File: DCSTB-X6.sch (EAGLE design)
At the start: 5 parts

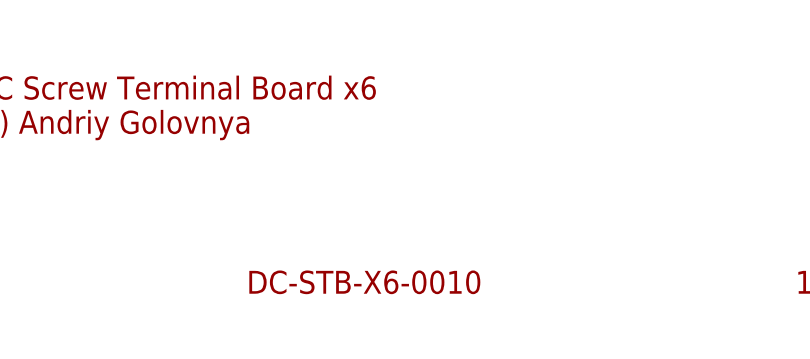
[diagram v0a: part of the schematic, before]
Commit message: Changed board texts. Generated CAM files. Generated PDF schematics.
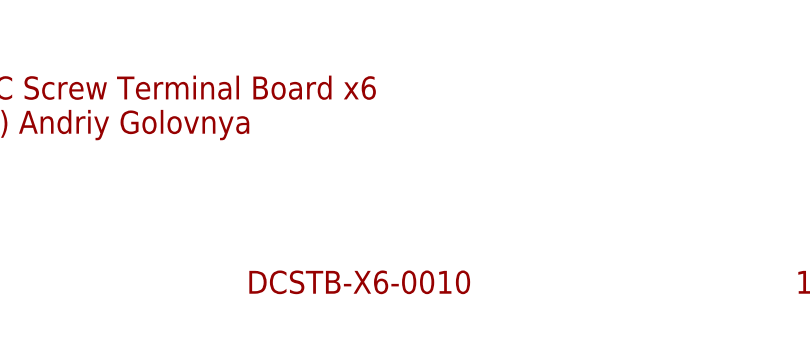
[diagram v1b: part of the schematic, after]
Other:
- note added: "DCSTB-X6-0010"
- note removed: "DC-STB-X6-0010"
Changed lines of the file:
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@@
 <sheet>
 <plain>
-<text x="195.58" y="7.62" size="2.54" layer="94">DC-STB-X6-0010</text>
+<text x="195.58" y="7.62" size="2.54" layer="94">DCSTB-X6-0010</text>
 <text x="256.54" y="7.62" size="2.54" layer="94">1.0</text>
 <text x="165.1" y="25.4" size="2.54" layer="94">DC Screw Terminal Board x6
